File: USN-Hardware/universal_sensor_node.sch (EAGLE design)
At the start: 19 parts, among them IC2 741G3157DCKR, J2 USB-MICROB, U2 ATMEGA328PB-AU, Y1 TSX-3225EPSON_TSX-3225_16.000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

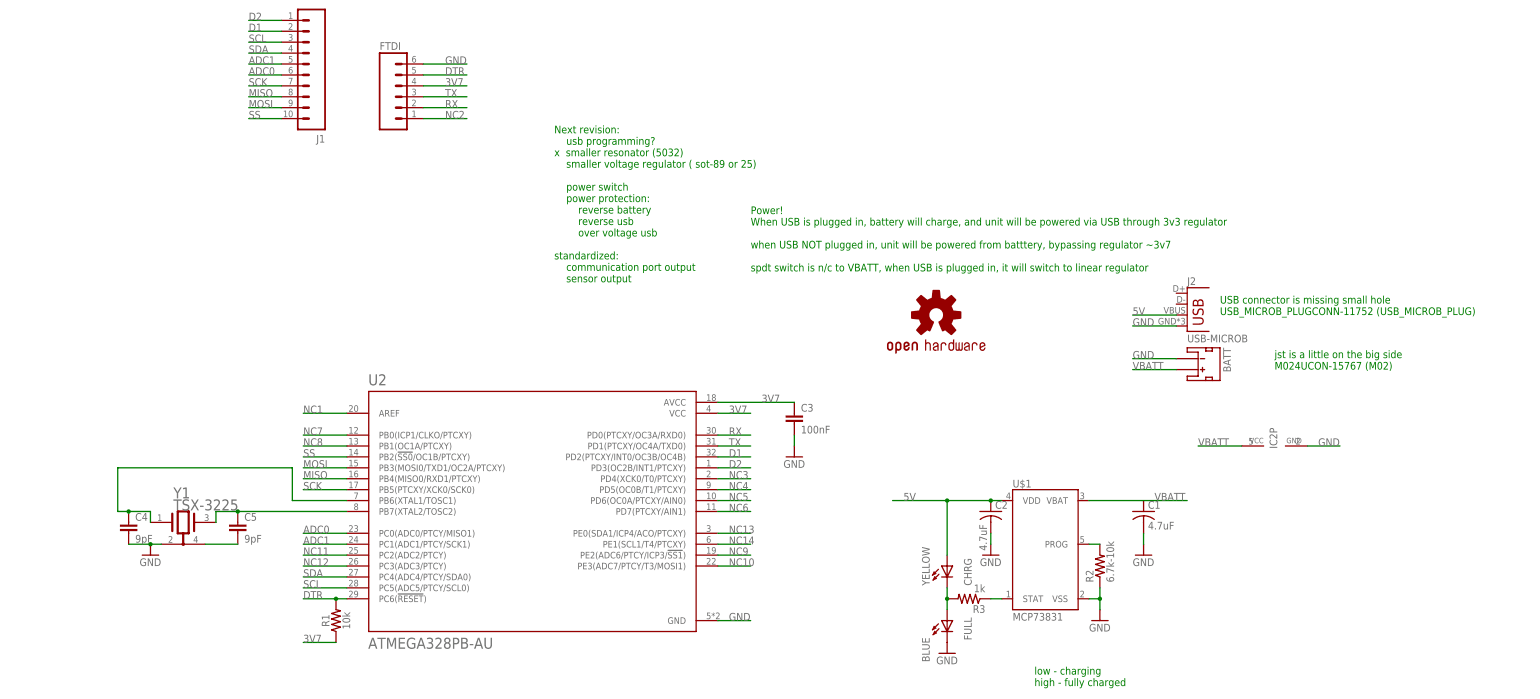
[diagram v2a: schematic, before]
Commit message: copied all all schematic components to project library.  Cleaned up schematic.
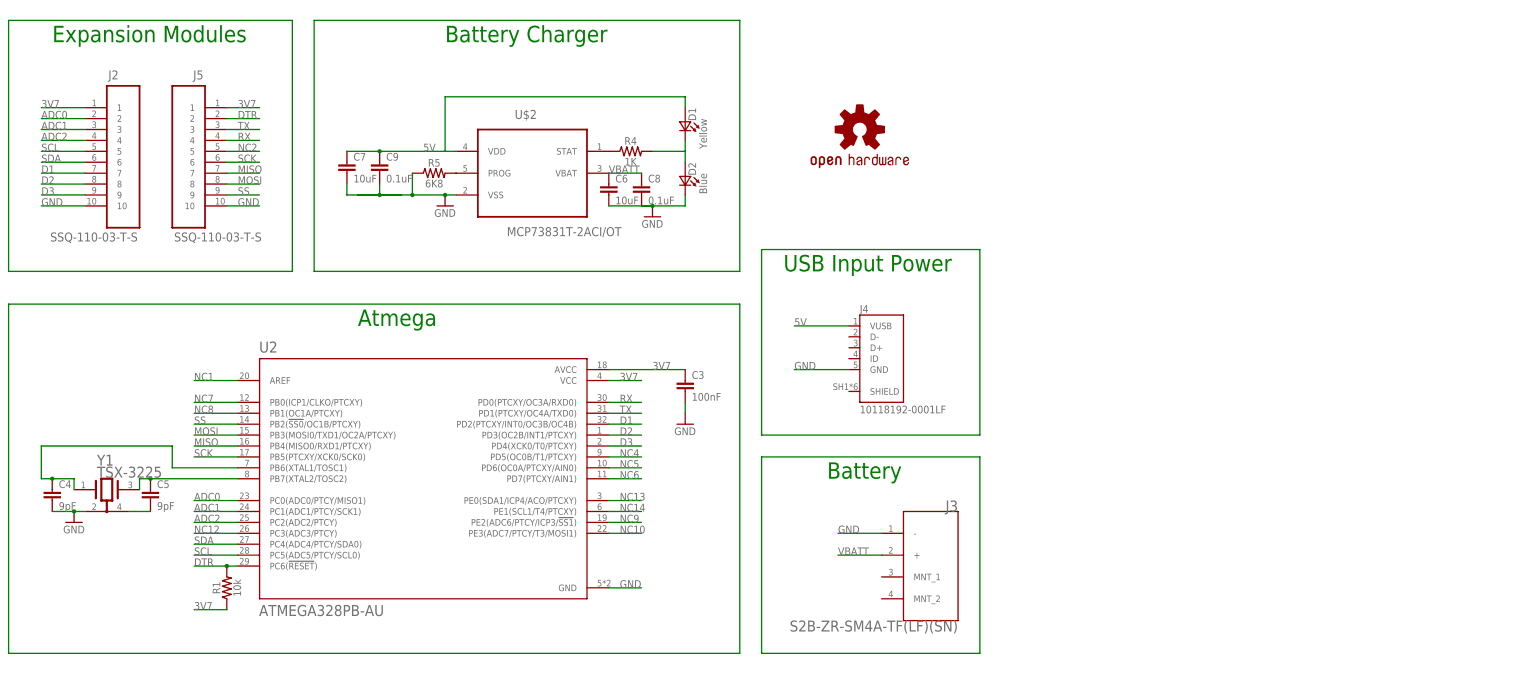
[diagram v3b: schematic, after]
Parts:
- removed BATT: (no value), SparkFun-Connectors:JST_2MM_MALE
- removed BLUE: FULL, led:LEDCHIPLED_0603
- removed C1, C2: 4.7uF, rcl:C-USC0603
- removed FTDI: (no value), SparkFun-Connectors:M06NO_SILK_FEMALE_PTH
- removed IC2: 741G3157DCKR, 74xx-little-de:741G3157DCKR
- removed J1: (no value), SparkFun-Connectors:M10NO_SILK_PTH_FEMALE
- removed R2: 6.7k-10k, rcl:R-US_R0603
- removed R3: 1k, rcl:R-US_R0603
- removed U$1: MCP73831, GeekAmmo:MCP73831
- removed YELLOW: CHRG, led:LEDCHIPLED_0603
- added C6, C7: 10uF, universal_sensor_node:CAP_0603_10UF
- added C8, C9: 0.1uF, universal_sensor_node:CAP_0603_0.1UF
- added D1: Yellow, universal_sensor_node:LTST-C191KSKT
- added D2: Blue, universal_sensor_node:LTST-C193TBKT-5A
- added J3: JST_S2B-ZR-SM4A-TF_LF_SNJST_S2B-ZR-SM4A-TF_LF_SN_0_0, universal_sensor_node:JST_S2B-ZR-SM4A-TF_LF_SNJST_S2B-ZR-SM4A-TF_LF_SN_0_0
- added J4: 10118192-0001LF, universal_sensor_node:10118192-0001LF
- added J5: SSQ-110-03-T-S, universal_sensor_node:SSQ-110-03-T-S
- added R4: 1K, universal_sensor_node:RES_0603_1K_1%_.1W-0603-1/10W-1%
- added R5: 6K8, universal_sensor_node:RES_0603_6.8K_1%_.1W-0603-1/10W-1%
- added U$2: MCP73831T-2ACI/OT, universal_sensor_node:MCP73831T-2ACI/OT
- J2: value USB-MICROB -> SSQ-110-03-T-S; device SparkFun-Connectors:USB-MICROB -> universal_sensor_node:SSQ-110-03-T-S
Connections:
- removed net N$1: R3.1, U$1.STAT
- removed net N$2: BLUE.A, R3.2, YELLOW.C
- removed net N$82: R2.2, U$1.PROG
- removed net NC11: U2.PC2(ADC2/PTCY)
- removed net NC3: U2.PD4(XCK0/T0/PTCXY)
- new net ADC2: J2.4, U2.PC2(ADC2/PTCY)
- new net D3: J2.9, U2.PD4(XCK0/T0/PTCXY)
- new net N$10: R4.1, U$2.STAT
- new net N$11: D1.K2, D2.A2, R4.2
- new net N$3: R5.2, U$2.PROG
- net 3V7: now also J2.1, J5.1; no longer FTDI.4
- net 5V: now also C7.1, C9.1, D1.A2, J4.VUSB, U$2.VDD; no longer C2.1, J2.VBUS, U$1.VDD, YELLOW.A
- net ADC0: now also J2.2; no longer J1.6
- net ADC1: now also J2.3; no longer J1.5
- net D1: now also J2.7; no longer J1.2
- net D2: now also J2.8; no longer J1.1
- net DTR: now also J5.2; no longer FTDI.5
- net GND: now also C6.2, C7.2, C8.2, C9.2, D2.K2, J2.10, J3.-, J4.GND, J5.10, R5.1, U$2.VSS; no longer BATT.-, BLUE.C, C1.2, C2.2, FTDI.6, IC2P.GND, J2.GND, R2.1, U$1.VSS
- net MISO: now also J5.7; no longer J1.8
- net MOSI: now also J5.8; no longer J1.9
- net NC2: now also J5.5; no longer FTDI.1
- net RX: now also J5.4; no longer FTDI.2
- net SCK: now also J5.6; no longer J1.7
- net SCL: now also J2.5; no longer J1.3
- net SDA: now also J2.6; no longer J1.4
- net SS: now also J5.9; no longer J1.10
- net TX: now also J5.3; no longer FTDI.3
- net VBATT: now also C6.1, C8.1, J3.+, U$2.VBAT; no longer BATT.+, C1.1, IC2P.VCC, U$1.VBAT
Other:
- note added: "Atmega"
- note added: "Battery"
- note added: "Battery Charger"
- note added: "Expansion Modules"
- note added: "USB Input Power"
- note removed: "Next revision: usb programming? x smaller resonator (5032) smaller voltage regulator ( sot-89 or 25) power switch power protection: reverse battery reverse usb over voltage usb standardized: communication port output sensor output"
- note removed: "Power! When USB is plugged in, battery will charge, and unit will be powered via USB through 3v3 regulator when USB NOT plugged in, unit will be powered from batttery, bypassing regulator ~3v7 spdt switch is n/c to VBATT, when USB is plugged in, it will switch to linear regulator"
- note removed: "USB connector is missing small hole USB_MICROB_PLUGCONN-11752 (USB_MICROB_PLUG)"
- note removed: "jst is a little on the big side M024UCON-15767 (M02)"
- note removed: "low - charging high - fully charged"
- moved on the sheet: C3, C4, C5, R1, U2, Y1

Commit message: schematic capture done, board layout done, and everything is routed.
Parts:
- removed U$2: MCP73831T-2ACI/OT, universal_sensor_node:MCP73831T-2ACI/OT
- added U1: MCP73831T-2ACI/OT, universal_sensor_node:MCP73831T-2ACI/OT
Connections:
- removed net N$3: R5.2, U$2.PROG
- removed net N$4: C5.2, Y1.2_GND
- removed net VBATT: C6.1, C8.1, J3.+, U$2.VBAT
- new net STAT: R4.1, U1.STAT
- net 3V7: now also C6.1, C8.1, J3.+, U1.VBAT
- net 5V: now also U1.VDD; no longer U$2.VDD
- net GND: now also C5.2, U1.VSS, Y1.2_GND; no longer U$2.VSS
- net N$10: now also R5.2, U1.PROG; no longer R4.1, U$2.STAT
- net RX: now also J5.3; no longer J5.4
- net SCL: now also J2.6; no longer J2.5
- net SDA: now also J2.5; no longer J2.6
- net TX: now also J5.4; no longer J5.3
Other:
- moved on the sheet: R4
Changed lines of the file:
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@@
 <part name="C5" library="universal_sensor_node" deviceset="9PF-50V(0603)" device="" value="9pF"/>
 <part name="R1" library="universal_sensor_node" deviceset="RES_0603_10K_1%_.1W" device="-0603-1/10W-1%" value="10k"/>
-<part name="U$2" library="universal_sensor_node" deviceset="MCP73831T-2ACI/OT" device=""/>
 <part name="C6" library="universal_sensor_node" deviceset="CAP_0603_10UF" device="" value="10uF"/>
 <part name="C8" library="universal_sensor_node" deviceset="CAP_0603_0.1UF" device="" value="0.1uF"/>
@@
 <part name="J2" library="universal_sensor_node" deviceset="SSQ-110-03-T-S" device=""/>
 <part name="J5" library="universal_sensor_node" deviceset="SSQ-110-03-T-S" device=""/>
+<part name="U1" library="universal_sensor_node" deviceset="MCP73831T-2ACI/OT" device=""/>
+<part name="GND1" library="supply1" deviceset="GND" device=""/>
 </parts>
 <sheets>
@@
 <attribute name="VALUE" x="101.6" y="60.96" size="1.778" layer="96"/>
 </instance>
-<instance part="GND8" gate="1" x="-38.1" y="40.64" smashed="yes">
-<attribute name="VALUE" x="-40.64" y="38.1" size="1.778" layer="96"/>
+<instance part="GND8" gate="1" x="-35.56" y="40.64" smashed="yes">
+<attribute name="VALUE" x="-38.1" y="38.1" size="1.778" layer="96"/>
 </instance>
 <instance part="LOGO1" gate="G$1" x="144.78" y="132.08" smashed="yes"/>
@@
 <attribute name="VALUE" x="-1.016" y="25.4" size="1.778" layer="96" font="vector" rot="R90" align="top-center"/>
 </instance>
-<instance part="U$2" gate="A" x="68.58" y="124.46" smashed="yes">
-<attribute name="NAME" x="64.457259375" y="134.5378" size="2.08681875" layer="95" ratio="10" rot="SR0"/>
-<attribute name="VALUE" x="62.62743125" y="107.2637" size="2.085940625" layer="96" ratio="10" rot="SR0"/>
-</instance>
 <instance part="C6" gate="G$1" x="86.36" y="116.84" smashed="yes">
 <attribute name="NAME" x="87.884" y="119.761" size="1.778" layer="95"/>
@@
 <attribute name="VALUE" x="109.22" y="121.91575" size="1.78096875" layer="96" rot="MR270"/>
 </instance>
-<instance part="R4" gate="G$1" x="91.44" y="127" smashed="yes">
-<attribute name="NAME" x="91.44" y="128.524" size="1.778" layer="95" font="vector" align="bottom-center"/>
-<attribute name="VALUE" x="91.44" y="125.476" size="1.778" layer="96" font="vector" align="top-center"/>
+<instance part="R4" gate="G$1" x="96.52" y="127" smashed="yes">
+<attribute name="NAME" x="96.52" y="128.524" size="1.778" layer="95" font="vector" align="bottom-center"/>
+<attribute name="VALUE" x="96.52" y="125.476" size="1.778" layer="96" font="vector" align="top-center"/>
 </instance>
 <instance part="R5" gate="G$1" x="45.72" y="121.92" smashed="yes">
@@
 <attribute name="NAME" x="-7.9756" y="143.7386" size="2.0828" layer="95" ratio="10" rot="SMR0"/>
 <attribute name="VALUE" x="5.5626" y="106.0196" size="2.0828" layer="96" ratio="10" rot="SMR0"/>
+</instance>
+<instance part="U1" gate="G$1" x="68.58" y="124.46" smashed="yes">
+<attribute name="NAME" x="64.457259375" y="134.5378" size="2.08681875" layer="95" ratio="10" rot="SR0"/>
+<attribute name="VALUE" x="62.62743125" y="107.2637" size="2.085940625" layer="96" ratio="10" rot="SR0"/>
+</instance>
+<instance part="GND1" gate="1" x="-25.4" y="40.64" smashed="yes">
+<attribute name="VALUE" x="-27.94" y="38.1" size="1.778" layer="96"/>
 </instance>
 </instances>
@@
 <net name="SDA" class="0">
 <segment>
-<wire x1="-35.56" y1="124.46" x2="-45.72" y2="124.46" width="0.1524" layer="91"/>
-<label x="-45.72" y="124.46" size="1.778" layer="95"/>
-<pinref part="J2" gate="A" pin="6"/>
-</segment>
-<segment>
 <wire x1="-10.16" y1="35.56" x2="0" y2="35.56" width="0.1524" layer="91"/>
 <pinref part="U2" gate="G$1" pin="PC4(ADC4/PTCY/SDA0)"/>
 <label x="-10.16" y="35.56" size="1.778" layer="95"/>
 </segment>
-</net>
-<net name="SCL" class="0">
-<segment>
+<segment>
+<pinref part="J2" gate="A" pin="5"/>
 <wire x1="-35.56" y1="127" x2="-45.72" y2="127" width="0.1524" layer="91"/>
 <label x="-45.72" y="127" size="1.778" layer="95"/>
-<pinref part="J2" gate="A" pin="5"/>
-</segment>
+</segment>
+</net>
+<net name="SCL" class="0">
 <segment>
 <wire x1="-10.16" y1="33.02" x2="0" y2="33.02" width="0.1524" layer="91"/>
@@
 <label x="-10.16" y="33.02" size="1.778" layer="95"/>
 </segment>
+<segment>
+<pinref part="J2" gate="A" pin="6"/>
+<wire x1="-35.56" y1="124.46" x2="-45.72" y2="124.46" width="0.1524" layer="91"/>
+<label x="-45.72" y="124.46" size="1.778" layer="95"/>
+</segment>
 </net>
 <net name="NC9" class="0">
@@
 <net name="RX" class="0">
 <segment>
-<wire x1="-2.54" y1="129.54" x2="5.08" y2="129.54" width="0.1524" layer="91"/>
-<label x="0" y="129.54" size="1.778" layer="95"/>
-<pinref part="J5" gate="A" pin="4"/>
-</segment>
-<segment>
 <wire x1="86.36" y1="68.58" x2="93.98" y2="68.58" width="0.1524" layer="91"/>
 <pinref part="U2" gate="G$1" pin="PD0(PTCXY/OC3A/RXD0)"/>
 <label x="88.9" y="68.58" size="1.778" layer="95"/>
 </segment>
-</net>
-<net name="TX" class="0">
-<segment>
+<segment>
+<pinref part="J5" gate="A" pin="3"/>
 <wire x1="-2.54" y1="132.08" x2="5.08" y2="132.08" width="0.1524" layer="91"/>
 <label x="0" y="132.08" size="1.778" layer="95"/>
-<pinref part="J5" gate="A" pin="3"/>
-</segment>
+</segment>
+</net>
+<net name="TX" class="0">
 <segment>
 <wire x1="86.36" y1="66.04" x2="93.98" y2="66.04" width="0.1524" layer="91"/>
 <pinref part="U2" gate="G$1" pin="PD1(PTCXY/OC4A/TXD0)"/>
 <label x="88.9" y="66.04" size="1.778" layer="95"/>
+</segment>
+<segment>
+<pinref part="J5" gate="A" pin="4"/>
+<wire x1="-2.54" y1="129.54" x2="5.08" y2="129.54" width="0.1524" layer="91"/>
+<label x="0" y="129.54" size="1.778" layer="95"/>
 </segment>
 </net>
@@
 <pinref part="J5" gate="A" pin="1"/>
 </segment>
+<segment>
+<wire x1="149.86" y1="33.02" x2="139.7" y2="33.02" width="0.1524" layer="91"/>
+<label x="139.7" y="33.02" size="1.778" layer="95"/>
+<pinref part="J3" gate="G$0" pin="+"/>
+</segment>
+<segment>
+<pinref part="C6" gate="G$1" pin="1"/>
+<pinref part="C8" gate="G$1" pin="1"/>
+<wire x1="86.36" y1="121.92" x2="93.98" y2="121.92" width="0.1524" layer="91"/>
+<label x="86.36" y="121.92" size="1.778" layer="95"/>
+<pinref part="U1" gate="G$1" pin="VBAT"/>
+<junction x="86.36" y="121.92"/>
+</segment>
 </net>
 <net name="NC1" class="0">
@@
 </segment>
 <segment>
-<pinref part="U$2" gate="A" pin="VDD"/>
 <wire x1="50.8" y1="127" x2="48.26" y2="127" width="0.1524" layer="91"/>
 <pinref part="C7" gate="G$1" pin="1"/>
@@
 <pinref part="D1" gate="G$1" pin="A2"/>
 <label x="43.18" y="127" size="1.778" layer="95"/>
+<pinref part="U1" gate="G$1" pin="VDD"/>
 </segment>
 </net>
@@
 <pinref part="C4" gate="G$1" pin="2"/>
 <pinref part="Y1" gate="G$0" pin="1_GND"/>
-<wire x1="-43.18" y1="43.18" x2="-38.1" y2="43.18" width="0.1524" layer="91"/>
+<wire x1="-43.18" y1="43.18" x2="-35.56" y2="43.18" width="0.1524" layer="91"/>
 <pinref part="GND8" gate="1" pin="GND"/>
-<wire x1="-38.1" y1="43.18" x2="-35.56" y2="43.18" width="0.1524" layer="91"/>
-<junction x="-38.1" y="43.18"/>
+<junction x="-35.56" y="43.18"/>
 </segment>
 <segment>
 <pinref part="R5" gate="G$1" pin="1"/>
-<pinref part="U$2" gate="A" pin="VSS"/>
 <wire x1="40.64" y1="121.92" x2="40.64" y2="116.84" width="0.1524" layer="91"/>
 <wire x1="40.64" y1="116.84" x2="48.26" y2="116.84" width="0.1524" layer="91"/>
@@
 <pinref part="C9" gate="G$1" pin="2"/>
 <wire x1="33.02" y1="119.38" x2="33.02" y2="116.84" width="0.1524" layer="91"/>
+<pinref part="U1" gate="G$1" pin="VSS"/>
 </segment>
 <segment>
@@
 <pinref part="J5" gate="A" pin="10"/>
 </segment>
+<segment>
+<pinref part="Y1" gate="G$0" pin="2_GND"/>
+<pinref part="C5" gate="G$1" pin="2"/>
+<wire x1="-25.4" y1="43.18" x2="-20.32" y2="43.18" width="0.1524" layer="91"/>
+<pinref part="GND1" gate="1" pin="GND"/>
+<junction x="-25.4" y="43.18"/>
+</segment>
 </net>
 <net name="NC2" class="0">
@@
 <label x="0" y="127" size="1.778" layer="95"/>
 <pinref part="J5" gate="A" pin="5"/>
-</segment>
-</net>
-<net name="VBATT" class="0">
-<segment>
-<wire x1="149.86" y1="33.02" x2="139.7" y2="33.02" width="0.1524" layer="91"/>
-<label x="139.7" y="33.02" size="1.778" layer="95"/>
-<pinref part="J3" gate="G$0" pin="+"/>
-</segment>
-<segment>
-<pinref part="U$2" gate="A" pin="VBAT"/>
-<pinref part="C6" gate="G$1" pin="1"/>
-<pinref part="C8" gate="G$1" pin="1"/>
-<wire x1="86.36" y1="121.92" x2="93.98" y2="121.92" width="0.1524" layer="91"/>
-<label x="86.36" y="121.92" size="1.778" layer="95"/>
 </segment>
 </net>
@@
 </segment>
 </net>
-<net name="N$4" class="0">
-<segment>
-<pinref part="Y1" gate="G$0" pin="2_GND"/>
-<pinref part="C5" gate="G$1" pin="2"/>
-<wire x1="-25.4" y1="43.18" x2="-20.32" y2="43.18" width="0.1524" layer="91"/>
-</segment>
-</net>
-<net name="N$3" class="0">
-<segment>
-<pinref part="U$2" gate="A" pin="PROG"/>
-<pinref part="R5" gate="G$1" pin="2"/>
-</segment>
-</net>
 <net name="N$6" class="0">
 <segment>
@@
 </segment>
 </net>
-<net name="N$10" class="0">
-<segment>
-<pinref part="U$2" gate="A" pin="STAT"/>
-<pinref part="R4" gate="G$1" pin="1"/>
-</segment>
-</net>
 <net name="N$11" class="0">
 <segment>
 <pinref part="R4" gate="G$1" pin="2"/>
-<wire x1="96.52" y1="127" x2="104.14" y2="127" width="0.1524" layer="91"/>
+<wire x1="101.6" y1="127" x2="104.14" y2="127" width="0.1524" layer="91"/>
 <pinref part="D1" gate="G$1" pin="K2"/>
 <wire x1="104.14" y1="127" x2="104.14" y2="129.54" width="0.1524" layer="91"/>
@@
 </segment>
 </net>
+<net name="STAT" class="0">
+<segment>
+<pinref part="R4" gate="G$1" pin="1"/>
+<pinref part="U1" gate="G$1" pin="STAT"/>
+<wire x1="91.44" y1="127" x2="86.36" y2="127" width="0.1524" layer="91"/>
+<label x="86.36" y="127" size="1.778" layer="95"/>
+</segment>
+</net>
+<net name="N$10" class="0">
+<segment>
+<pinref part="R5" gate="G$1" pin="2"/>
+<pinref part="U1" gate="G$1" pin="PROG"/>
+</segment>
+</net>

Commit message: looks good to me.  Placed order with oshpark
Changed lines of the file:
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@@
 <wire x1="48.26" y1="127" x2="33.02" y2="127" width="0.1524" layer="91"/>
 <wire x1="33.02" y1="127" x2="25.4" y2="127" width="0.1524" layer="91"/>
-<junction x="33.02" y="127"/>
 <wire x1="48.26" y1="127" x2="48.26" y2="139.7" width="0.1524" layer="91"/>
 <wire x1="48.26" y1="139.7" x2="104.14" y2="139.7" width="0.1524" layer="91"/>
@@
 <label x="43.18" y="127" size="1.778" layer="95"/>
 <pinref part="U1" gate="G$1" pin="VDD"/>
+<junction x="48.26" y="127"/>
+<junction x="33.02" y="127"/>
 </segment>
 </net>
@@
 </segment>
 <segment>
+<pinref part="U1" gate="G$1" pin="VSS"/>
+<wire x1="48.26" y1="116.84" x2="50.8" y2="116.84" width="0.1524" layer="91"/>
+<pinref part="GND5" gate="1" pin="GND"/>
+<pinref part="C7" gate="G$1" pin="2"/>
+<wire x1="48.26" y1="116.84" x2="40.64" y2="116.84" width="0.1524" layer="91"/>
+<wire x1="40.64" y1="116.84" x2="33.02" y2="116.84" width="0.1524" layer="91"/>
+<wire x1="33.02" y1="116.84" x2="25.4" y2="116.84" width="0.1524" layer="91"/>
+<wire x1="25.4" y1="116.84" x2="25.4" y2="119.38" width="0.1524" layer="91"/>
+<pinref part="C9" gate="G$1" pin="2"/>
+<wire x1="33.02" y1="119.38" x2="33.02" y2="116.84" width="0.1524" layer="91"/>
 <pinref part="R5" gate="G$1" pin="1"/>
 <wire x1="40.64" y1="121.92" x2="40.64" y2="116.84" width="0.1524" layer="91"/>
-<wire x1="40.64" y1="116.84" x2="48.26" y2="116.84" width="0.1524" layer="91"/>
-<wire x1="48.26" y1="116.84" x2="50.8" y2="116.84" width="0.1524" layer="91"/>
-<wire x1="25.4" y1="116.84" x2="33.02" y2="116.84" width="0.1524" layer="91"/>
-<pinref part="GND5" gate="1" pin="GND"/>
-<wire x1="33.02" y1="116.84" x2="40.64" y2="116.84" width="0.1524" layer="91"/>
-<pinref part="C7" gate="G$1" pin="2"/>
-<wire x1="25.4" y1="119.38" x2="25.4" y2="116.84" width="0.1524" layer="91"/>
-<pinref part="C9" gate="G$1" pin="2"/>
-<wire x1="33.02" y1="119.38" x2="33.02" y2="116.84" width="0.1524" layer="91"/>
-<pinref part="U1" gate="G$1" pin="VSS"/>
+<junction x="33.02" y="116.84"/>
+<junction x="40.64" y="116.84"/>
+<junction x="48.26" y="116.84"/>
 </segment>
 <segment>
 <pinref part="C6" gate="G$1" pin="2"/>
 <pinref part="C8" gate="G$1" pin="2"/>
-<wire x1="86.36" y1="114.3" x2="96.52" y2="114.3" width="0.1524" layer="91"/>
+<wire x1="86.36" y1="114.3" x2="93.98" y2="114.3" width="0.1524" layer="91"/>
 <pinref part="GND6" gate="1" pin="GND"/>
+<wire x1="93.98" y1="114.3" x2="96.52" y2="114.3" width="0.1524" layer="91"/>
 <wire x1="96.52" y1="114.3" x2="93.98" y2="114.3" width="0.1524" layer="91"/>
 <junction x="96.52" y="114.3"/>
@@
 <wire x1="93.98" y1="114.3" x2="104.14" y2="114.3" width="0.1524" layer="91"/>
 <wire x1="104.14" y1="114.3" x2="104.14" y2="116.84" width="0.1524" layer="91"/>
+<junction x="93.98" y="114.3"/>
 </segment>
 <segment>
@@
 </segment>
 </net>
-<net name="N$6" class="0">
-<segment>
-<wire x1="38.1" y1="116.84" x2="27.94" y2="116.84" width="0.1524" layer="91"/>
-</segment>
-</net>
-<net name="N$7" class="0">
-<segment>
-<junction x="33.02" y="116.84"/>
-</segment>
-</net>
-<net name="N$8" class="0">
-<segment>
-<junction x="40.64" y="116.84"/>
-</segment>
-</net>
-<net name="N$9" class="0">
-<segment>
-<junction x="48.26" y="116.84"/>
-</segment>
-</net>
 <net name="N$11" class="0">
 <segment>
@@
 <pinref part="D2" gate="G$1" pin="A2"/>
 <wire x1="104.14" y1="127" x2="104.14" y2="124.46" width="0.1524" layer="91"/>
+<junction x="104.14" y="127"/>
 </segment>
 </net>
